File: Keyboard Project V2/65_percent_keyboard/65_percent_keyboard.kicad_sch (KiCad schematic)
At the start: 5 parts, among them U1 ATmega32A-P, Y1 16MHz

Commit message: updated directory
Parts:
- added SW1: SW_Push, symbol Switch:SW_Push
- C1, C2: value C -> 22uF
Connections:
- net +5V: now also U1.30 (AVCC)
- net GND: now also SW1.1
- net at R1.1, U1.9 (~{RESET}): now also SW1.2
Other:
- moved on the sheet: R1
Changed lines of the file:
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@@
 (kicad_sch (version 20230121) (generator eeschema)
   (paper "A4")
-  (junction (at 66.04 143.51) (diameter 0) (color 0 0 0 0)
+  (junction (at 50.8 40.64) (diameter 0) (color 0 0 0 0)
+  )
+  (junction (at 21.59 53.34) (diameter 0) (color 0 0 0 0)
   )
   (junction (at 38.1 57.15) (diameter 0) (color 0 0 0 0)
@@
   (junction (at 66.04 35.56) (diameter 0) (color 0 0 0 0)
   )
-  (junction (at 21.59 57.15) (diameter 0) (color 0 0 0 0)
-  )
   (junction (at 38.1 49.53) (diameter 0) (color 0 0 0 0)
   )
-  (wire (pts (xy 21.59 49.53) (xy 21.59 57.15))
-    (stroke (width 0) (type default))
-  )
-  (wire (pts (xy 66.04 143.51) (xy 21.59 143.51))
-    (stroke (width 0) (type default))
-  )
-  (wire (pts (xy 50.8 45.72) (xy 50.8 35.56))
-    (stroke (width 0) (type default))
-  )
-  (wire (pts (xy 62.23 35.56) (xy 66.04 35.56))
-    (stroke (width 0) (type default))
-  )
-  (wire (pts (xy 50.8 35.56) (xy 54.61 35.56))
-    (stroke (width 0) (type default))
-  )
-  (wire (pts (xy 66.04 139.7) (xy 66.04 143.51))
+  (wire (pts (xy 68.58 35.56) (xy 68.58 38.1))
+    (stroke (width 0) (type default))
+  )
+  (wire (pts (xy 21.59 49.53) (xy 21.59 53.34))
+    (stroke (width 0) (type default))
+  )
+  (wire (pts (xy 50.8 40.64) (xy 50.8 45.72))
+    (stroke (width 0) (type default))
+  )
+  (wire (pts (xy 17.78 53.34) (xy 21.59 53.34))
+    (stroke (width 0) (type default))
+  )
+  (wire (pts (xy 21.59 53.34) (xy 21.59 57.15))
+    (stroke (width 0) (type default))
+  )
+  (wire (pts (xy 66.04 35.56) (xy 68.58 35.56))
     (stroke (width 0) (type default))
   )
@@
     (stroke (width 0) (type default))
   )
+  (wire (pts (xy 44.45 40.64) (xy 50.8 40.64))
+    (stroke (width 0) (type default))
+  )
   (wire (pts (xy 66.04 35.56) (xy 66.04 38.1))
     (stroke (width 0) (type default))
   )
+  (wire (pts (xy 50.8 36.83) (xy 50.8 40.64))
+    (stroke (width 0) (type default))
+  )
   (wire (pts (xy 38.1 49.53) (xy 50.8 49.53))
     (stroke (width 0) (type default))
   )
-  (wire (pts (xy 66.04 143.51) (xy 66.04 148.59))
-    (stroke (width 0) (type default))
-  )
-  (wire (pts (xy 21.59 143.51) (xy 21.59 57.15))
+  (wire (pts (xy 66.04 139.7) (xy 66.04 148.59))
     (stroke (width 0) (type default))
   )
   (wire (pts (xy 66.04 29.21) (xy 66.04 35.56))
+    (stroke (width 0) (type default))
+  )
+  (wire (pts (xy 34.29 40.64) (xy 30.48 40.64))
     (stroke (width 0) (type default))
   )
@@
         (path "/317806f0-7832-447d-a362-c03f416f1932"
           (reference "Y1") (unit 1)
+        )
+      )
+    )
+  )
+  (symbol (lib_id "power:GND") (at 30.48 40.64 0) (unit 1)
+    (in_bom yes) (on_board yes) (dnp no) (fields_autoplaced)
+    (property "Reference" "#PWR05" (at 30.48 46.99 0)
+      (effects (font (size 1.27 1.27)) hide)
+    )
+    (property "Value" "GND" (at 30.48 45.72 0)
+      (effects (font (size 1.27 1.27)))
+    )
+    (property "Footprint" "" (at 30.48 40.64 0)
+      (effects (font (size 1.27 1.27)) hide)
+    )
+    (property "Datasheet" "" (at 30.48 40.64 0)
+      (effects (font (size 1.27 1.27)) hide)
+    )
+    (pin "1")
+    (instances
+      (project "65_percent_keyboard"
+        (path "/317806f0-7832-447d-a362-c03f416f1932"
+          (reference "#PWR05") (unit 1)
         )
       )
@@
       (effects (font (size 1.27 1.27)))
     )
-    (property "Value" "C" (at 25.4 54.61 90)
+    (property "Value" "22uF" (at 25.4 54.61 90)
       (effects (font (size 1.27 1.27)))
     )
@@
         (path "/317806f0-7832-447d-a362-c03f416f1932"
           (reference "C2") (unit 1)
+        )
+      )
+    )
+  )
+  (symbol (lib_id "Switch:SW_Push") (at 39.37 40.64 0) (unit 1)
+    (in_bom yes) (on_board yes) (dnp no) (fields_autoplaced)
+    (property "Reference" "SW1" (at 39.37 33.02 0)
+      (effects (font (size 1.27 1.27)))
+    )
+    (property "Value" "SW_Push" (at 39.37 35.56 0)
+      (effects (font (size 1.27 1.27)))
+    )
+    (property "Footprint" "" (at 39.37 35.56 0)
+      (effects (font (size 1.27 1.27)) hide)
+    )
+    (property "Datasheet" "~" (at 39.37 35.56 0)
+      (effects (font (size 1.27 1.27)) hide)
+    )
+    (pin "1")
+    (pin "2")
+    (instances
+      (project "65_percent_keyboard"
+        (path "/317806f0-7832-447d-a362-c03f416f1932"
+          (reference "SW1") (unit 1)
+        )
+      )
+    )
+  )
+  (symbol (lib_id "power:GND") (at 17.78 53.34 270) (unit 1)
+    (in_bom yes) (on_board yes) (dnp no) (fields_autoplaced)
+    (property "Reference" "#PWR03" (at 11.43 53.34 0)
+      (effects (font (size 1.27 1.27)) hide)
+    )
+    (property "Value" "GND" (at 13.97 53.34 90)
+      (effects (font (size 1.27 1.27)) (justify right))
+    )
+    (property "Footprint" "" (at 17.78 53.34 0)
+      (effects (font (size 1.27 1.27)) hide)
+    )
+    (property "Datasheet" "" (at 17.78 53.34 0)
+      (effects (font (size 1.27 1.27)) hide)
+    )
+    (pin "1")
+    (instances
+      (project "65_percent_keyboard"
+        (path "/317806f0-7832-447d-a362-c03f416f1932"
+          (reference "#PWR03") (unit 1)
         )
       )
@@
       (effects (font (size 1.27 1.27)))
     )
-    (property "Value" "C" (at 25.4 45.72 90)
+    (property "Value" "22uF" (at 25.4 45.72 90)
       (effects (font (size 1.27 1.27)))
     )
@@
     )
   )
+  (symbol (lib_id "power:+5V") (at 50.8 29.21 0) (unit 1)
+    (in_bom yes) (on_board yes) (dnp no) (fields_autoplaced)
+    (property "Reference" "#PWR04" (at 50.8 33.02 0)
+      (effects (font (size 1.27 1.27)) hide)
+    )
+    (property "Value" "+5V" (at 50.8 24.13 0)
+      (effects (font (size 1.27 1.27)))
+    )
+    (property "Footprint" "" (at 50.8 29.21 0)
+      (effects (font (size 1.27 1.27)) hide)
+    )
+    (property "Datasheet" "" (at 50.8 29.21 0)
+      (effects (font (size 1.27 1.27)) hide)
+    )
+    (pin "1")
+    (instances
+      (project "65_percent_keyboard"
+        (path "/317806f0-7832-447d-a362-c03f416f1932"
+          (reference "#PWR04") (unit 1)
+        )
+      )
+    )
+  )
   (symbol (lib_id "power:GND") (at 66.04 148.59 0) (unit 1)
     (in_bom yes) (on_board yes) (dnp no) (fields_autoplaced)
@@
     )
   )
-  (symbol (lib_id "Device:R_US") (at 58.42 35.56 90) (unit 1)
-    (in_bom yes) (on_board yes) (dnp no) (fields_autoplaced)
-    (property "Reference" "R1" (at 58.42 29.21 90)
-      (effects (font (size 1.27 1.27)))
-    )
-    (property "Value" "10k" (at 58.42 31.75 90)
-      (effects (font (size 1.27 1.27)))
-    )
-    (property "Footprint" "" (at 58.674 34.544 90)
-      (effects (font (size 1.27 1.27)) hide)
-    )
-    (property "Datasheet" "~" (at 58.42 35.56 0)
-      (effects (font (size 1.27 1.27)) hide)
-    )
+  (symbol (lib_id "Device:R_US") (at 50.8 33.02 180) (unit 1)
+    (in_bom yes) (on_board yes) (dnp no) (fields_autoplaced)
+    (property "Reference" "R1" (at 53.34 31.75 0)
+      (effects (font (size 1.27 1.27)) (justify right))
+    )
+    (property "Value" "10k" (at 53.34 34.29 0)
+      (effects (font (size 1.27 1.27)) (justify right))
+    )
+    (property "Footprint" "" (at 49.784 32.766 90)
+      (effects (font (size 1.27 1.27)) hide)
+    )
+    (property "Datasheet" "~" (at 50.8 33.02 0)
+      (effects (font (size 1.27 1.27)) hide)
+    )

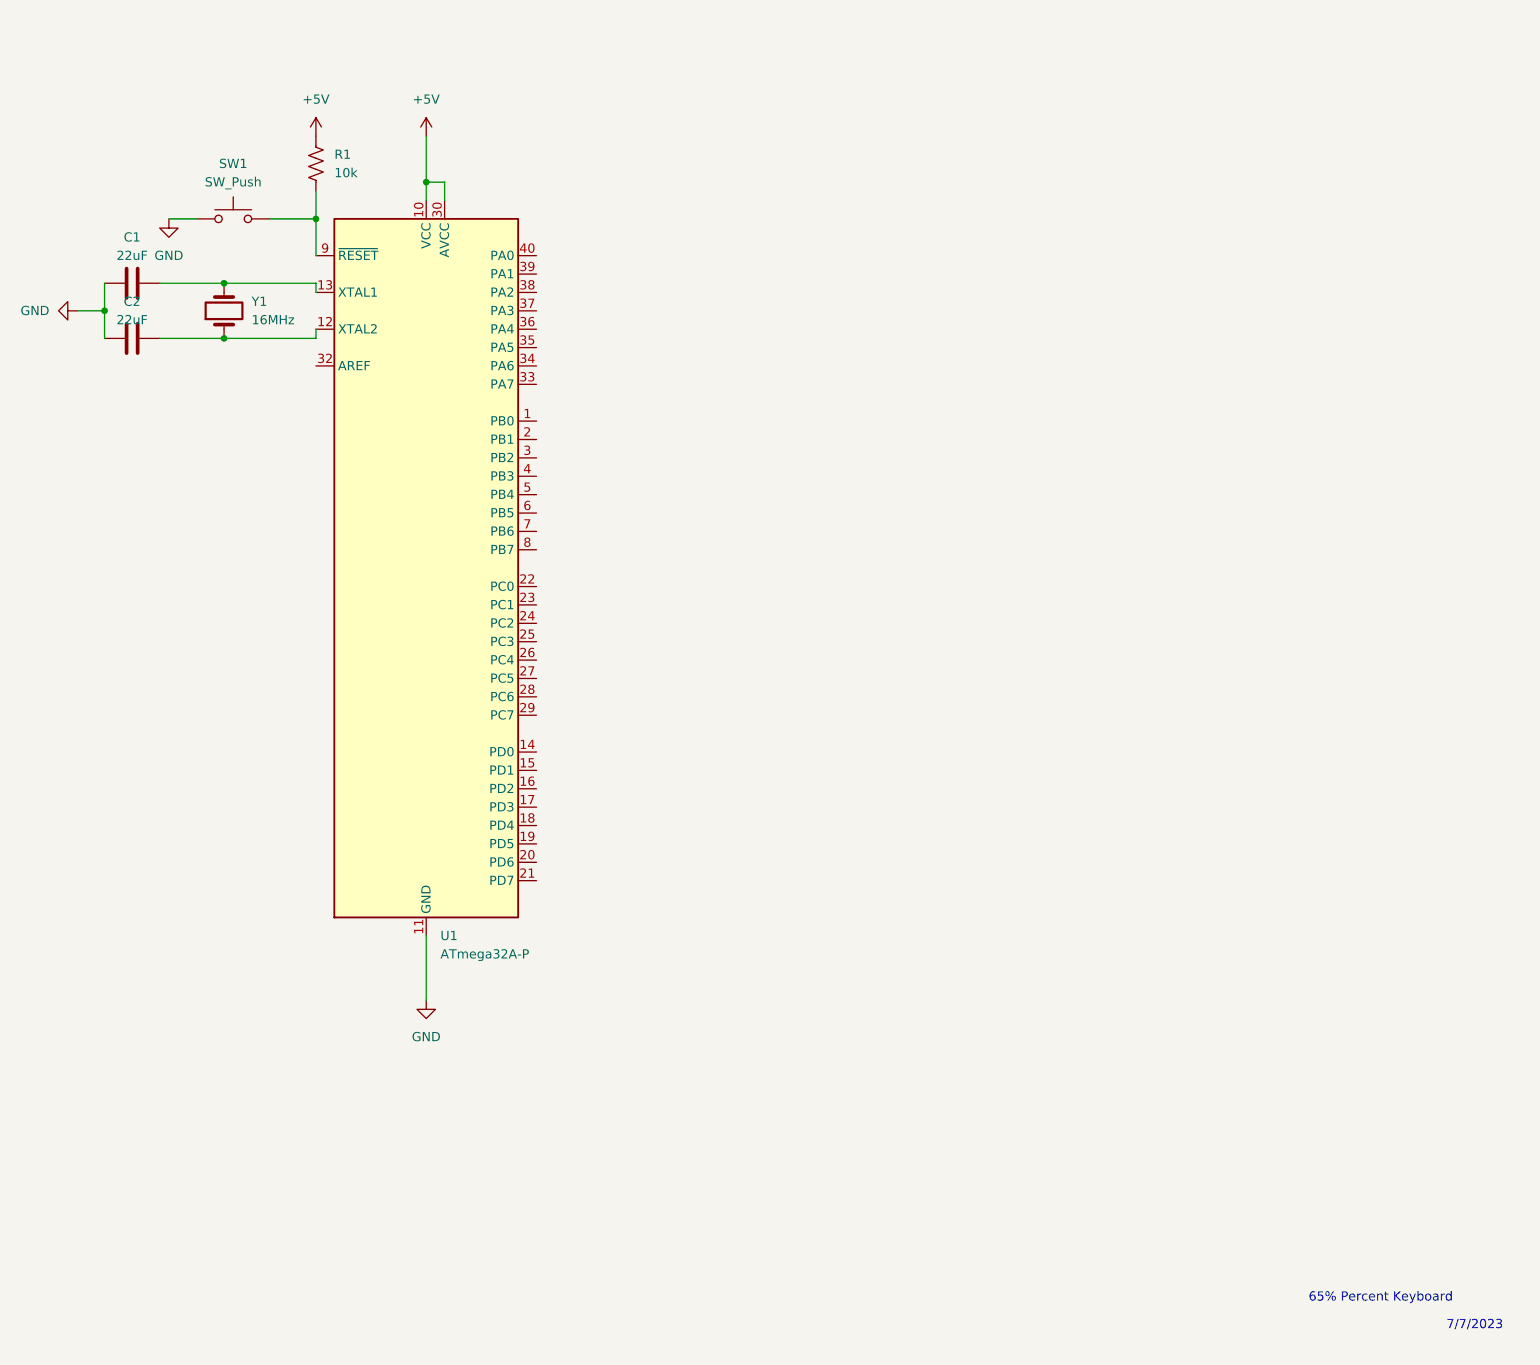
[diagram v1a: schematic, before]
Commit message: updated keyboard project 2, just need to add the switches and minor tweaks
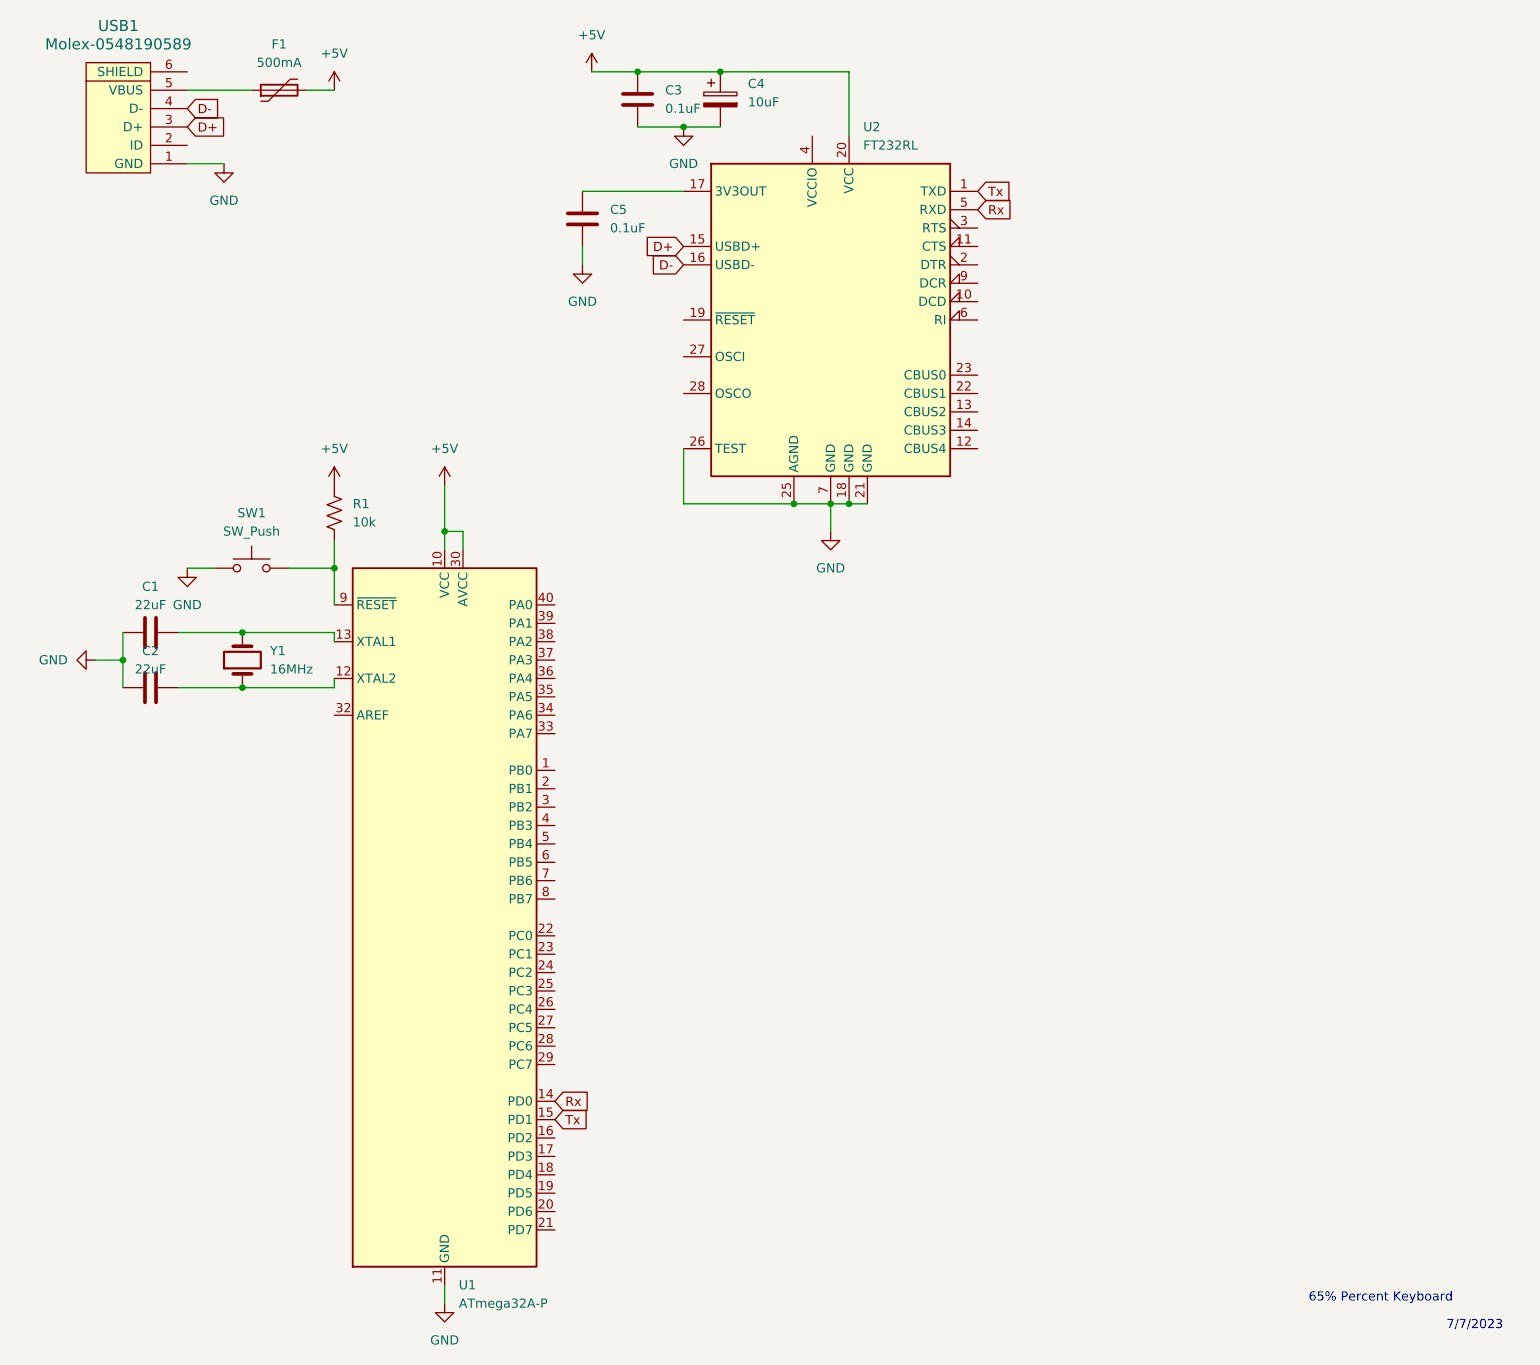
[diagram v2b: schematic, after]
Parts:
- added C3, C5: 0.1uF, symbol Device:C
- added C4: 10uF, symbol Device:C_Polarized
- added F1: 500mA, symbol Device:Polyfuse
- added U2: FT232RL, Package_SO:SSOP-28_5.3x10.2mm_P0.65mm, symbol Interface_USB:FT232RL
- added USB1: Molex-0548190589, symbol random-keyboard-parts:Molex-0548190589
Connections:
- net +5V: now also C3.1, C4.1, F1.2, U2.20 (VCC)
- net GND: now also C3.2, C4.2, C5.2, U2.18 (GND), U2.21 (GND), U2.25 (AGND), U2.26 (TEST), U2.7 (GND), USB1.1 (GND)
- net Rx: now reaches U1.14 (PD0)
- net Rx: now also U2.5 (RXD)
- net Tx: now reaches U1.15 (PD1)
- net Tx: now also U2.1 (TXD)
- new net: F1.1, USB1.5 (VBUS)
- new net: C5.1, U2.17 (3V3OUT)
- new net D+: U2.15 (USBD+), USB1.3 (D+)
- new net D-: U2.16 (USBD-), USB1.4 (D-)
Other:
- moved on the sheet: C1, C2, R1, SW1, U1, Y1
